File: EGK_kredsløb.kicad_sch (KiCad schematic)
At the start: 33 parts, among them J1 Conn_01x03, U1 INA114AP, U2 MCP6004, U3 MCP6004, U4 MCP6004, U5 MCP6004

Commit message: finished schematic, missing AUX
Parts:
- removed C2: 10μ, Capacitor_THT:CP_Radial_D6.3mm_P2.50mm, symbol Device:C_Polarized
- removed C9: 100n, Capacitor_THT:C_Rect_L7.0mm_W2.0mm_P5.00mm, symbol Device:C
- removed R6, R7: 15k, Resistor_THT:R_Axial_DIN0207_L6.3mm_D2.5mm_P10.16mm_Horizontal, symbol Device:R
- removed unit 1 of U2
- removed U3, U4, U5: MCP6004, Package_DIP:DIP-14_W7.62mm_Socket_LongPads, symbol Amplifier_Operational:MCP6004
- added C10, C6: 100n, Capacitor_THT:C_Rect_L7.0mm_W2.0mm_P5.00mm, symbol Device:C
- added C11: 10n, Capacitor_THT:C_Rect_L7.0mm_W2.0mm_P5.00mm, symbol Device:C
- added C4: 1μ, Capacitor_THT:CP_Radial_D6.3mm_P2.50mm, symbol Device:C_Polarized
- added H1, H2, H3, H4: MountingHole, MountingHole:MountingHole_3.2mm_M3_ISO7380, symbol Mechanical:MountingHole
- added J1: USB4085-GF-A_REVB, connector:GCT_USB4085-GF-A_REVB, symbol USB4085-GF-A_REVB:USB4085-GF-A_REVB
- added J2, J3, J5: Conn_01x01_Pin, Connector_PinHeader_2.54mm:PinHeader_1x01_P2.54mm_Vertical, symbol Connector:Conn_01x01_Pin
- added J6: Conn_01x06_Pin, Connector_PinHeader_2.54mm:PinHeader_1x06_P2.54mm_Vertical, symbol Connector:Conn_01x06_Pin
- added R1: 20, Resistor_THT:R_Axial_DIN0207_L6.3mm_D2.5mm_P10.16mm_Horizontal, symbol Device:R
- added R4: 15k, Resistor_THT:R_Axial_DIN0207_L6.3mm_D2.5mm_P10.16mm_Horizontal, symbol Device:R
- added TP1, TP10, TP11, TP12, TP13, TP14, TP16, TP18, TP19, TP2, TP20, TP21, TP22, TP3, TP4, TP5, TP6, TP7, TP8, TP9: TestPoint, TestPoint:TestPoint_Pad_D3.0mm, symbol Connector:TestPoint
- added U1: MCP6004, Package_DIP:DIP-14_W7.62mm_Socket_LongPads, symbol Amplifier_Operational:MCP6004
- added unit 2 of U2
- added unit 3 of U2
- added unit 4 of U2
- added U4: MCP3208, Package_DIP:DIP-16_W7.62mm_Socket_LongPads, symbol Analog_ADC:MCP3208
- C3: value 1μ -> 10μ
- J4: renamed from J1; footprint (none) -> Connector_PinHeader_2.54mm:PinHeader_1x03_P2.54mm_Vertical
- R5: value 20 -> 15k
- renumbered C5 to C1, C6 to C2, C4 to C5, C8 to C7, C7 to C8, C1 to C9, R4 to R10, R3 to R11, R14 to R12, R15 to R13, R2 to R14, R12 to R15, R9 to R2, R8 to R3, R10 to R6, R11 to R7, R13 to R8, R1 to R9, TP1 to TP15, TP2 to TP17, U1 to U3
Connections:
- net SIGNAL_INA is gone; now on net SIGNAL_AMP: C1.2
- net +5V: now also C3.1, L1.2, C10.1, C11.1, C6.1, R4.2, U1.4 (V+), U4.15 (Vref), U4.16 (Vdd); no longer L1.1
- net GND: now also C10.2, C11.2, C4.2, C6.2, J1.A1 (GND), J1.A12 (GND__1), J1.B1 (GND__2), J1.B12 (GND__3), J6.5 (Pin_5), J6.6 (Pin_6), R1.1, U1.11 (V-), U4.14 (AGND), U4.9 (DGND); no longer C3.2, J4.3 (Pin_3)
- net INA_OUT: now also U2.3 (+), TP20.1; no longer U2.5 (+)
- net L_ARM: now also TP12.1
- net R_ARM: now also TP11.1
- net R_LEG: now also J4.3 (Pin_3), TP10.1, TP19.1
- net RightLegDrive: now also U2.5 (+)
- net SIGNAL_AMP: now also U2.1, J2.1 (Pin_1), TP1.1, TP22.1; no longer U2.7
- net SIGNAL_HP: now also J3.1 (Pin_1), TP5.1, U1.6 (-), U1.7
- net SIGNAL_OUT: now also J5.1 (Pin_1), TP14.1, U2.8, U2.9 (-), U4.1 (CH0)
- net VGND: now also TP16.1, TP2.1, TP6.1, TP8.1, U1.1, U1.10 (+), U1.2 (-)
- net at C2.1, R2.2: now also TP3.1, TP4.1, U1.5 (+)
- net at C7.2, R7.1: now also TP9.1, U2.10 (+)
- net at R12.1, R13.2: now also TP18.1, U1.8
- net at R12.2, R8.1: now also U1.9 (-)
- net at R14.2, R15.1: now also U2.2 (-), TP21.1; no longer U2.6 (-)
- net at R8.2: now also TP13.1, U2.6 (-), U2.7
- net at C8.1, R6.1, R7.2: now also TP7.1
- net V_BIAS: now reaches R5.2
- net V_BIAS: now also C4.1, R4.1, U1.3 (+)
- new net: C3.2, R1.2
- new net 5V_USB: J1.A4 (VBUS), L1.1
- new net CHIP_SELECT: J6.4 (Pin_4), U4.10 (~{CS}/SHDN)
- new net DIGITAL_OUT: J6.2 (Pin_2), U4.12 (Dout)
- new net SERIAL_CLK: J6.1 (Pin_1), U4.13 (CLK)
- new net SERIAL_DATA_IN: J6.3 (Pin_3), U4.11 (Din)
- no-connect marks 0 -> 31
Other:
- note added: "ADC"
- note added: "Bias signal for singel ended opamp configuration Center signals around 2.5 V"
- note added: "Buffer (non-inverting 1x gain)"
- note added: "Gain Block"
- note added: "Gennemgå hvilke opamps der fysisk er samlet i den samme pakke. Der er 2 pakker i alt at anvende"
- note added: "Hvilken USB connector på input power"
- note added: "Hvilken connector til at programmere og til at flytte data fra adc til RPI husk ground"
- note added: "Højpas: 0.05 Hz"
- note added: "Input power and filtering from USB-C"
- note added: "Inverting amplifier"
- note added: "Lavpas 100Hz"
- note added: "Non-inverting 2x amplification 1 + Rfeedback/Rground = 1 + 10k/10k = 2"
- note added: "POWER"
- note added: "To do - Find alle de righte footprints (datablade, 3d modeller, evt. kig på digikeys hjemmeside efter komponent og ECAD modeller) - Indsæt test points og/eller pin headers hvor kredsløbet skal måles (alle inputs og outputs i blokke) - Find connector på input (USB) - Find connector på output (programmering (SPI) af ADC og output til RPI. Husk ground) - Verificer i "view symbol fields" at alle symb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"
- note added: "f_c = 1 / (2·π·√(240kΩ·470kΩ·10µF·10µF)) ≈ 0.05 Hz"
- note added: "f_c = 1 / (2·π·√(7.5kΩ·7.5kΩ·300nF·150nF)) ≈ 100 Hz"
- note added: "footprints til pin headers"
- note removed: "5V"
- note removed: "Instrumentationsforstærker forsat"
- note removed: "Strømforsyning"
- moved on the sheet: C1, C2, C5, C7, C8, C9, J4, R10, R11, R12, R13, R14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

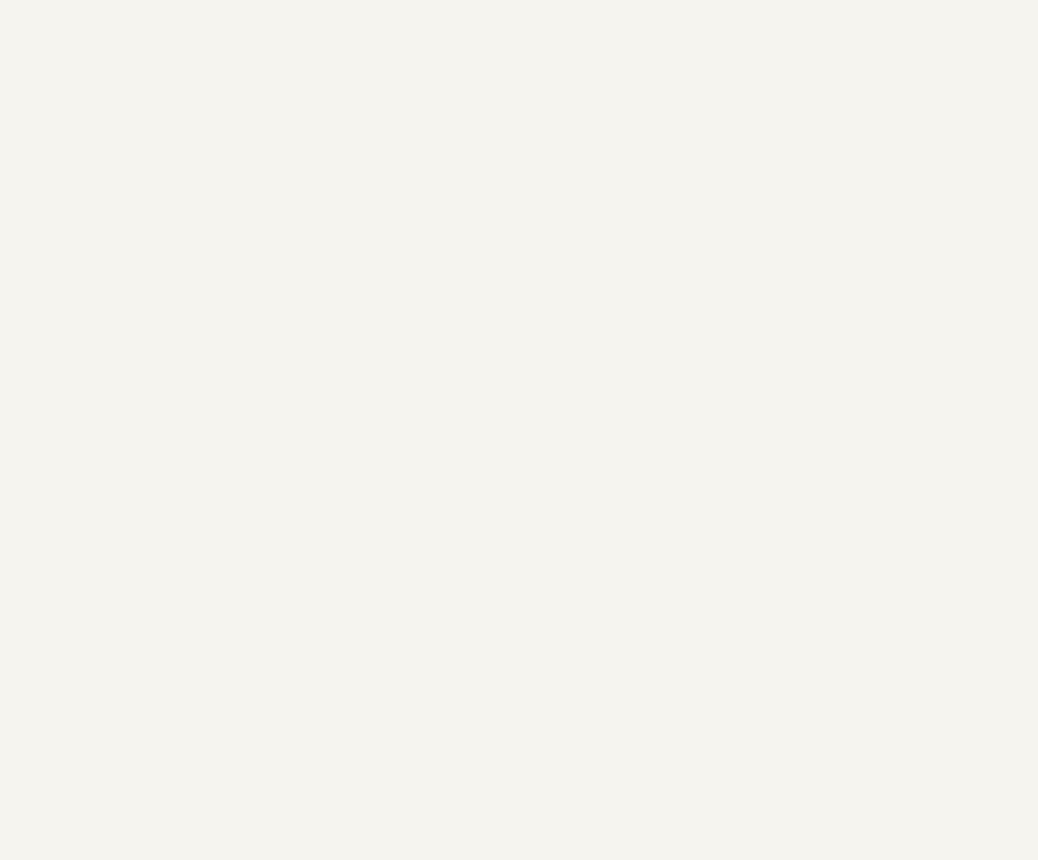
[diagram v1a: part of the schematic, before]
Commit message: opdateret med micro-usb samt 3.5mm audio jack til elektroder
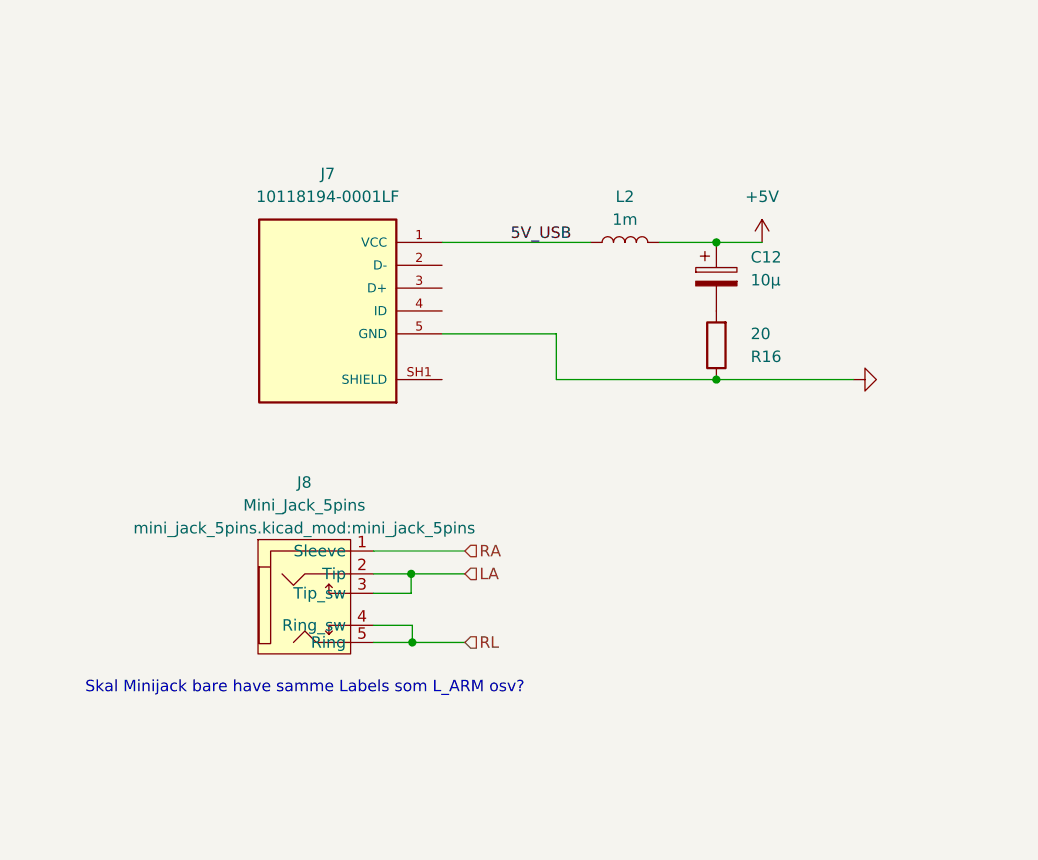
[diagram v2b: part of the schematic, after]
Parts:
- added C12: 10μ, Capacitor_THT:CP_Radial_D6.3mm_P2.50mm, symbol Device:C_Polarized
- added J7: 10118194-0001LF, connector:AMPHENOL_10118194-0001LF, symbol usbmicro:10118194-0001LF
- added J8: Mini_Jack_5pins, mini_jack_5pins.kicad_mod:mini_jack_5pins, symbol HFS_Library:Mini_Jack_5_pin
- added L2: 1m, Inductor_THT:L_Axial_L7.0mm_D3.3mm_P12.70mm_Horizontal_Fastron_MICC, symbol Device:L
- added R16: 20, Resistor_THT:R_Axial_DIN0207_L6.3mm_D2.5mm_P10.16mm_Horizontal, symbol Device:R
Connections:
- net +5V: now also C12.1, L2.2
- net 5V_USB: now also J7.1 (VCC), L2.1
- net GND: now also J7.5 (GND), R16.1
- new net: C12.2, R16.2
- new net: J7.SH1 (SHIELD), J7.SH2 (SHIELD), J7.SH3 (SHIELD), J7.SH4 (SHIELD), J7.SH5 (SHIELD), J7.SH6 (SHIELD)
- new net LA: J8.2 (Tip), J8.3 (Tip_sw)
- new net RA: J8.1 (Sleeve)
- new net RL: J8.4 (Ring_sw), J8.5 (Ring)
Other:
- note added: "Skal Minijack bare have samme Labels som L_ARM osv?"

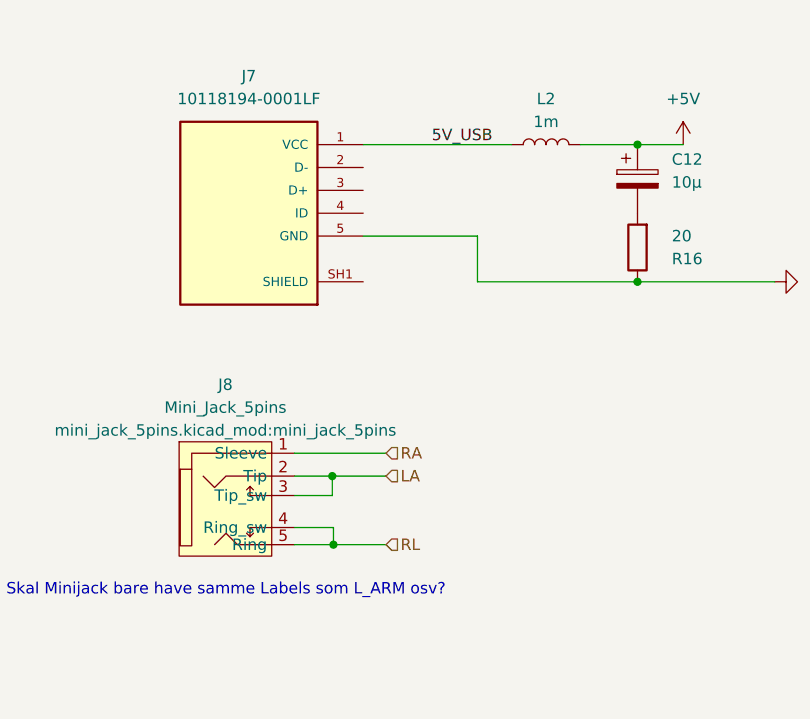
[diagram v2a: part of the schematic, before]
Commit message: ERC tjek, labels tilføjet til mini jack
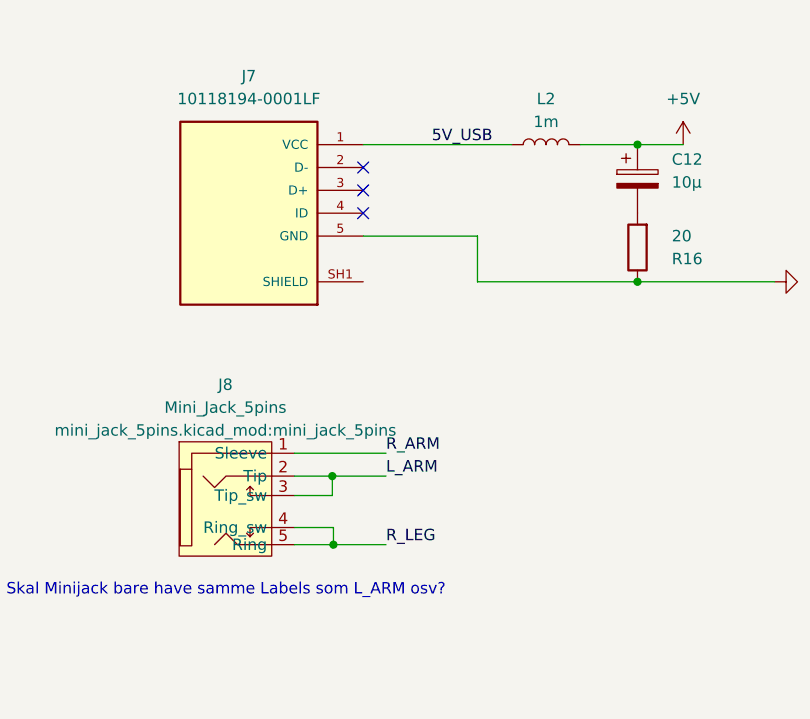
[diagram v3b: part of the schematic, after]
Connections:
- net LA is gone; now on net L_ARM: J8.2 (Tip), J8.3 (Tip_sw)
- net RA is gone; now on net R_ARM: J8.1 (Sleeve)
- net RL is gone; now on net R_LEG: J8.4 (Ring_sw), J8.5 (Ring)
- no-connect marks 31 -> 34
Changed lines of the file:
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@@
 	)
 	(no_connect
+		(at -55.88 35.56)
+	)
+	(no_connect
 		(at 274.32 149.86)
 	)
@@
 	)
 	(no_connect
+		(at -55.88 30.48)
+	)
+	(no_connect
 		(at 48.26 43.18)
 	)
@@
 	)
 	(no_connect
+		(at -55.88 33.02)
+	)
+	(no_connect
 		(at 48.26 53.34)
 	)
@@
 		)
 	)
+	(label "R_ARM"
+		(at -53.34 62.23 0)
+		(effects
+			(font
+				(size 1.27 1.27)
+			)
+			(justify left bottom)
+		)
+	)
 	(label "SIGNAL_AMP"
 		(at 398.78 58.42 180)
@@
 		)
 	)
+	(label "L_ARM"
+		(at -53.34 64.77 0)
+		(effects
+			(font
+				(size 1.27 1.27)
+			)
+			(justify left bottom)
+		)
+	)
 	(label "INA_OUT"
 		(at 345.44 55.88 0)
@@
 		)
 	)
-	(label "VGND"
-		(at 167.64 165.1 0)
+	(label "R_LEG"
+		(at -53.34 72.39 0)
 		(effects
 			(font
@@
 		)
 	)
-	(hierarchical_label "RA"
-		(shape input)
-		(at -53.34 62.23 0)
-		(effects
-			(font
-				(size 1.27 1.27)
-			)
-			(justify left)
-		)
-	)
-	(hierarchical_label "LA"
-		(shape input)
-		(at -53.34 64.77 0)
-		(effects
-			(font
-				(size 1.27 1.27)
-			)
-			(justify left)
-		)
-	)
-	(hierarchical_label "RL"
-		(shape input)
-		(at -53.34 72.39 0)
+	(label "VGND"
+		(at 167.64 165.1 0)
 		(effects
 			(font
 				(size 1.27 1.27)
 			)
-			(justify left)
+			(justify left bottom)
 		)
 	)

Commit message: Add layout floorplan ready for routing
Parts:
- removed C3: 10μ, Capacitor_THT:CP_Radial_D6.3mm_P2.50mm, symbol Device:C_Polarized
- removed J1: USB4085-GF-A_REVB, connector:GCT_USB4085-GF-A_REVB, symbol USB4085-GF-A_REVB:USB4085-GF-A_REVB
- removed J2, J3, J5: Conn_01x01_Pin, Connector_PinHeader_2.54mm:PinHeader_1x01_P2.54mm_Vertical, symbol Connector:Conn_01x01_Pin
- removed L1: 1m, Inductor_THT:L_Axial_L7.0mm_D3.3mm_P12.70mm_Horizontal_Fastron_MICC, symbol Device:L
- removed R1: 20, Resistor_THT:R_Axial_DIN0207_L6.3mm_D2.5mm_P10.16mm_Horizontal, symbol Device:R
- removed TP1, TP13, TP14, TP15, TP16, TP17, TP18, TP19, TP2, TP20, TP21, TP22, TP3, TP4, TP5, TP6, TP7, TP8, TP9: TestPoint, TestPoint:TestPoint_Pad_D3.0mm, symbol Connector:TestPoint
- added J102, J104: Conn_01x03, Connector_PinHeader_2.54mm:PinHeader_1x03_P2.54mm_Vertical, symbol Connector_Generic:Conn_01x03
- added J103, J111, J112: Conn_01x06_Pin, Connector_PinHeader_2.54mm:PinHeader_1x06_P2.54mm_Vertical, symbol Connector:Conn_01x06_Pin
- J108: renamed from J8; footprint mini_jack_5pins.kicad_mod:mini_jack_5pins -> connector:mini_jack_5pins
- renumbered C1 to C101, C2 to C102, C12 to C103, C4 to C104, C5 to C105, C6 to C106, C7 to C107, C8 to C108, C9 to C109, C10 to C110, C11 to C111, H1 to H101, H2 to H102, H3 to H103, H4 to H104, J7 to J101, J4 to J107, J6 to J110, L2 to L101, R16 to R101, R2 to R102, R3 to R103, R4 to R104, R5 to R105, R6 to R106, R7 to R107, R8 to R108, R9 to R109, R10 to R110, R11 to R111, R12 to R112, R13 to R113, R14 to R114, R15 to R115, TP10 to TP109, TP11 to TP110, TP12 to TP111, U2 to U101, U1 to U102, U3 to U103, U4 to U104
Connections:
- net +5V: now also J103.1 (Pin_1), J103.2 (Pin_2)
- net CHIP_SELECT: now also J111.4 (Pin_4)
- net DIGITAL_OUT: now also J111.2 (Pin_2)
- net GND: now also J101.SH1 (SHIELD), J101.SH2 (SHIELD), J101.SH3 (SHIELD), J101.SH4 (SHIELD), J101.SH5 (SHIELD), J101.SH6 (SHIELD), J103.5 (Pin_5), J103.6 (Pin_6), J111.5 (Pin_5), J111.6 (Pin_6)
- net INA_OUT: now also U101.12 (+), J102.3 (Pin_3); no longer U101.3 (+)
- net L_ARM: now also J107.2 (Pin_2), TP110.1; no longer J107.1 (Pin_1), TP111.1
- net R_ARM: now also J107.1 (Pin_1), J108.4 (Ring_sw), J108.5 (Ring), TP111.1; no longer J107.2 (Pin_2), J108.1 (Sleeve), TP110.1
- net R_LEG: now also J108.1 (Sleeve), J104.2 (Pin_2); no longer J108.4 (Ring_sw), J108.5 (Ring)
- net RightLegDrive: now also U102.9 (-), J104.3 (Pin_3); no longer U101.5 (+)
- net SERIAL_CLK: now also J111.1 (Pin_1)
- net SERIAL_DATA_IN: now also J111.3 (Pin_3)
- net SIGNAL_AMP: now also J112.6 (Pin_6); no longer C101.2, R115.2, U101.1
- net SIGNAL_OUT: now also J112.1 (Pin_1); no longer C108.2, U101.8, U101.9 (-), U104.1 (CH0)
- net V+IN: now also J102.1 (Pin_1)
- net V-IN: now also J102.2 (Pin_2)
- net VGND: now also U101.1, U101.2 (-), U102.6 (-), J103.3 (Pin_3), J103.4 (Pin_4); no longer U102.1, U102.10 (+), U102.2 (-)
- net V_BIAS: now also U101.3 (+); no longer U102.3 (+)
- net HP+: now reaches C102.1, R102.2
- net HP+: now also U102.3 (+), J112.2 (Pin_2); no longer U102.5 (+)
- net at R112.1, R113.2: now also U102.7; no longer U102.8
- net at R108.1, R112.2: now also U102.5 (+); no longer U102.9 (-)
- net LP+: now reaches U102.12 (+)
- net LP+: now also C107.2, R107.1, J112.4 (Pin_4)
- net ADC_IN: now reaches U102.13 (-)
- net ADC_IN: now also C108.2, U102.14, U104.1 (CH0)
- net at R114.2, R115.1: now also U101.13 (-); no longer U101.2 (-)
- net LP_IN: now reaches C108.1, R106.1, R107.2
- net LP_IN: now also J112.5 (Pin_5)
- net GAIN_BLOCK_OUT: now reaches U101.14
- net GAIN_BLOCK_OUT: now also C101.2, R115.2
- net SIGNAL_HP renamed HP_OUT
- net HP_OUT: now also U102.1, U102.2 (-), J112.3 (Pin_3); no longer U102.6 (-), U102.7
- new net: J104.1 (Pin_1), R108.2, U102.10 (+), U102.8
- now unconnected: U101.10 (+), U101.6 (-), U101.7
- no-connect marks 34 -> 16
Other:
- note added: "Mechanical"
- note added: "Unused amplifiers"
- note added: "brug 02x06"
- note added: "f_c = 1 / (2·π·√(R1·R2·C1·C2)) f_c = 1 / (2·π·√(7.5kΩ·7.5kΩ·300nF·150nF)) ≈ 100 Hz"
- note removed: "3.5mm audio-jack(mangler)"
- note removed: "Gennemgå hvilke opamps der fysisk er samlet i den samme pakke. Der er 2 pakker i alt at anvende"
- note removed: "Skal Minijack bare have samme Labels som L_ARM osv?"
- note removed: "f_c = 1 / (2·π·√(7.5kΩ·7.5kΩ·300nF·150nF)) ≈ 100 Hz"
- moved on the sheet: C103, C107, C108, C109, H101, H102, H103, H104, J101, J107, J108, J110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

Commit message: routed pcb
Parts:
- removed J110, J111: Conn_01x06_Pin, Connector_PinHeader_2.54mm:PinHeader_1x06_P2.54mm_Vertical, symbol Connector:Conn_01x06_Pin
- added D101: LED, LED_THT:LED_D5.0mm, symbol Device:LED
- added J105: Conn_02x06_Odd_Even, Connector_PinHeader_2.54mm:PinHeader_2x06_P2.54mm_Vertical, symbol Connector_Generic:Conn_02x06_Odd_Even
- added JP101: Jumper_2_Small_Bridged, Connector_PinHeader_2.54mm:PinHeader_1x02_P2.54mm_Vertical, symbol Jumper:Jumper_2_Small_Bridged
- added R116: 470, Resistor_THT:R_Axial_DIN0207_L6.3mm_D2.5mm_P10.16mm_Horizontal, symbol Device:R
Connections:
- net SIGNAL_AMP is gone; now on net ADC_IN: J112.6 (Pin_6)
- net SIGNAL_OUT is gone; now on net GAIN_BLOCK_OUT: J112.1 (Pin_1)
- net +5V: now also D101.2 (A)
- net 5V_USB: now also JP101.1 (A); no longer L101.1
- net CHIP_SELECT: now also J105.7 (Pin_7), J105.8 (Pin_8)
- net DIGITAL_OUT: now also J105.3 (Pin_3), J105.4 (Pin_4)
- net GND: now also J105.10 (Pin_10), J105.11 (Pin_11), J105.12 (Pin_12), J105.9 (Pin_9), R116.1
- net R_LEG: now also J104.1 (Pin_1); no longer J104.2 (Pin_2)
- net SERIAL_CLK: now also J105.1 (Pin_1), J105.2 (Pin_2)
- net SERIAL_DATA_IN: now also J105.5 (Pin_5), J105.6 (Pin_6)
- net at R108.2, U102.10 (+), U102.8: now also J104.2 (Pin_2); no longer J104.1 (Pin_1)
- new net: JP101.2 (B), L101.1
- new net: D101.1 (K), R116.2
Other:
- moved on the sheet: L101
